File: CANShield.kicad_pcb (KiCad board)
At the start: 4 copper layers, 70 x 59 mm, 92 parts, among them J101 Conn_02x19_Odd_Even, J102 Conn_02x19_Odd_Even, J103 Conn_01x04_Socket, J104 Conn_01x06_Socket, Q101 Si1308EDL, Q102 Si1308EDL, Q103 Si1308EDL, U101 TJA1443ATK/0Z, U102 BD2222G, U103 AT25SF081-XMHD-X, U104 MR20H40

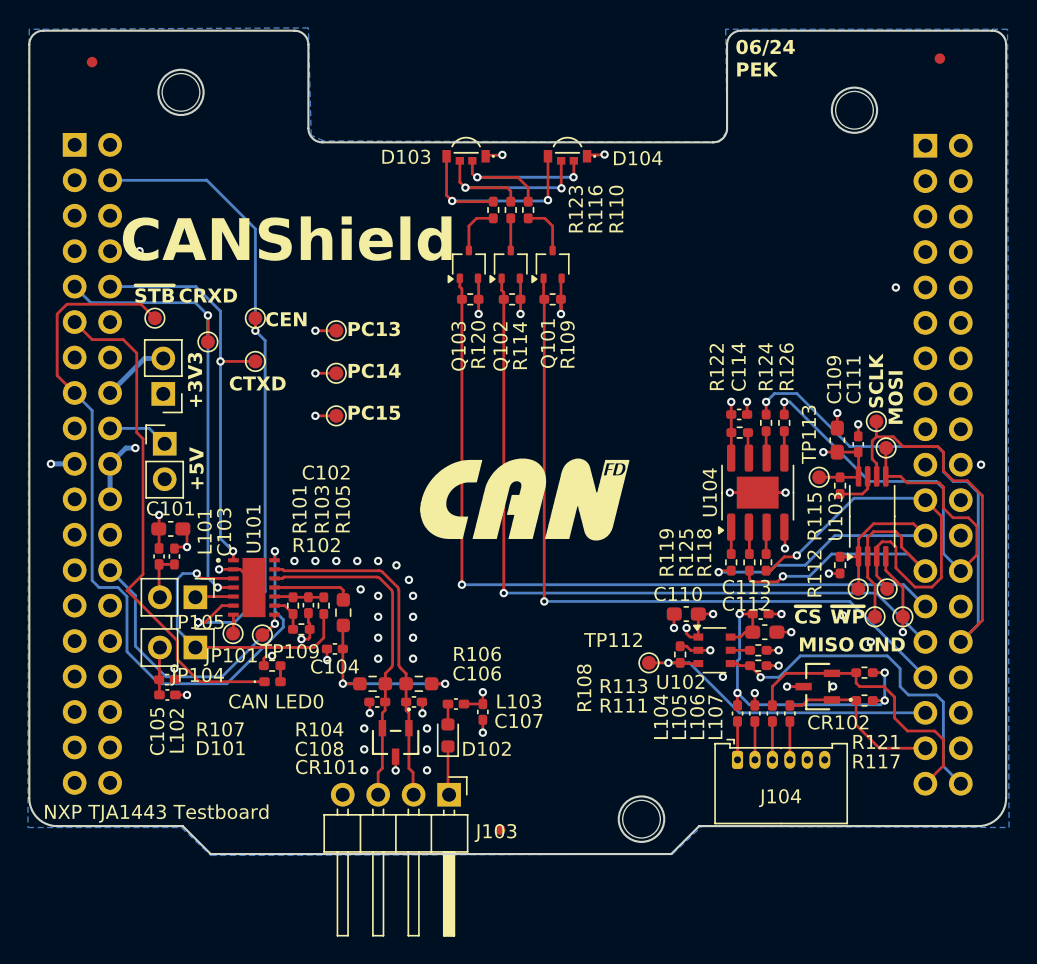
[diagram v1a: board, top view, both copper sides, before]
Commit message: Update BOM
Small changes on pcb layout and update BOM
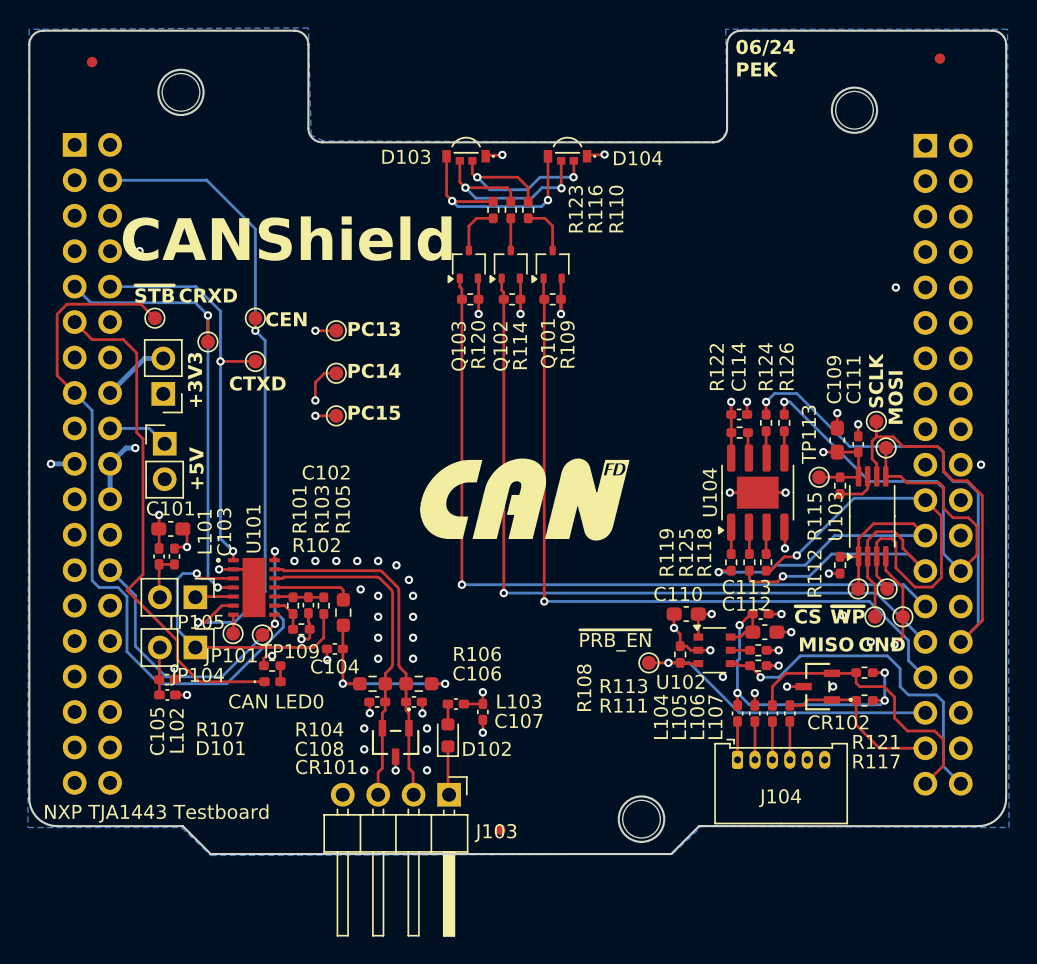
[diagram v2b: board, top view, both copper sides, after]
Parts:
- renumbered TP112 to ~{PRB_EN}
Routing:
- net GND: track 60.7 -> 63.5 mm
- net +5V: track 76.0 -> 74.2 mm, vias 4 -> 3
- net /LED0_RED: track 52.8 -> 53.6 mm
- net /PC14: track 31.3 -> 32.1 mm
- net Net-(D103-RK): track 14.6 -> 15.3 mm
- net /PC15: track 29.1 -> 28.5 mm
- net Net-(D103-GK): track 15.6 -> 16.2 mm
- net /~{WP}: track 30.3 -> 30.8 mm

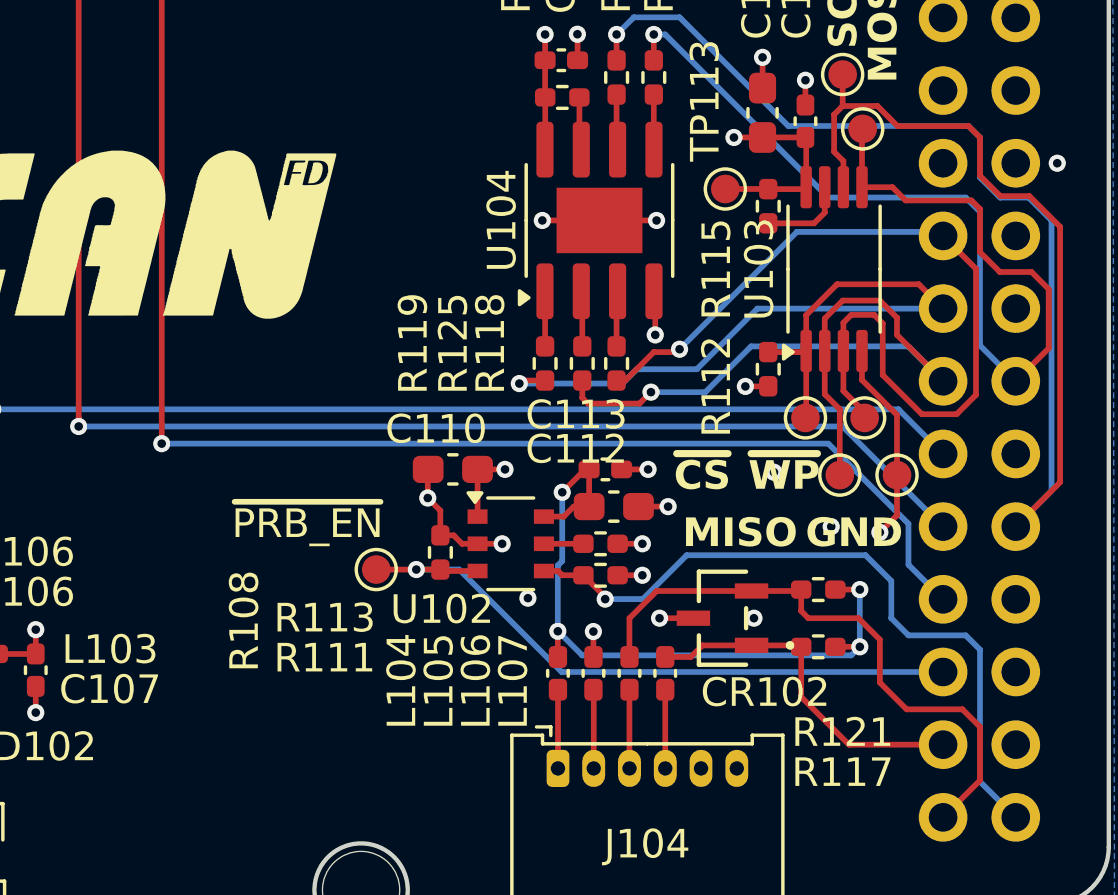
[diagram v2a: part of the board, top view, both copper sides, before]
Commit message: Add bew esd diode
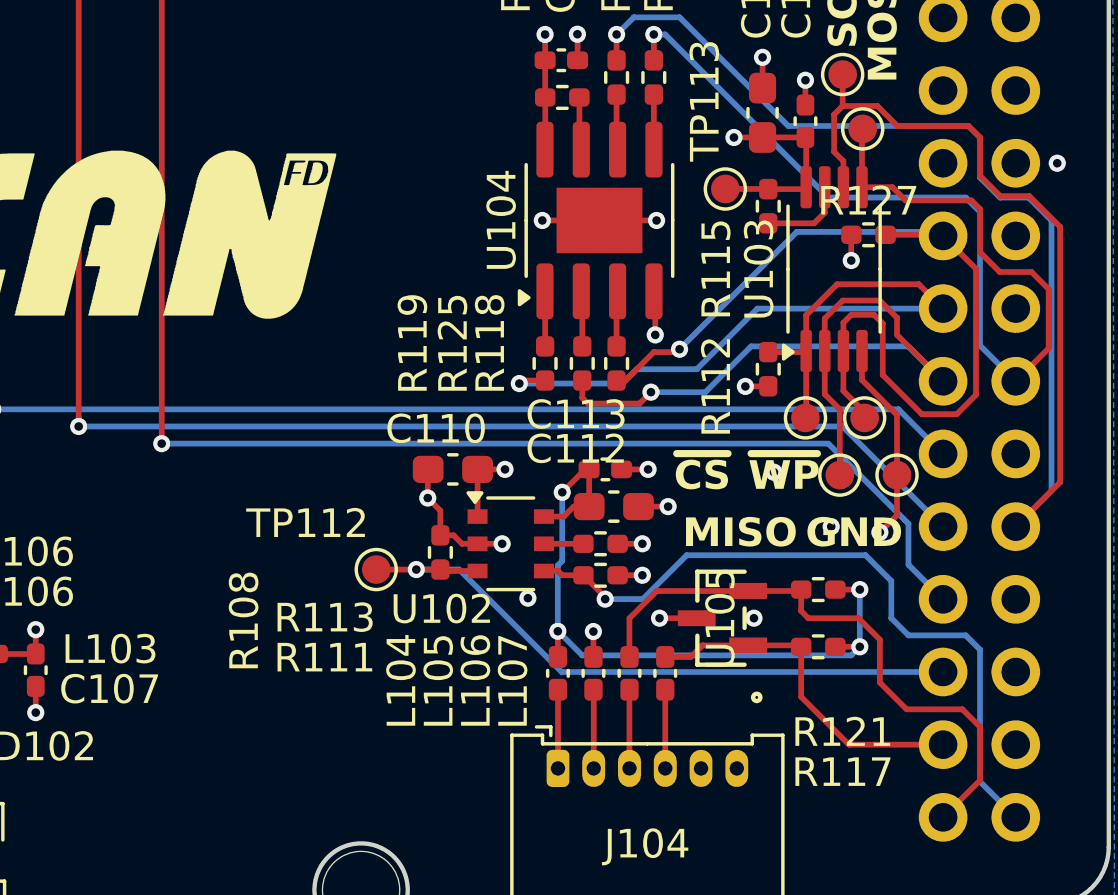
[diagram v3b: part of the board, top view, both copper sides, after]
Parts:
- removed CR102: PESD2CANFD27V-TR, PESD2CANFD27V-TR:SOT23_PESD2_NEX
- added R127: 100k, Resistor_SMD:R_0402_1005Metric_Pad0.72x0.64mm_HandSolder, F.Cu at (161.9, 101.6)
- added U105: PESD5V0S2BT, PESD5V:SOT23_NEX, F.Cu at (156.7, 115.0)
- R116: value 1k -> 680
- R123: value 1k -> 340
- U102: value BD2222G -> BD22441G-C
- U103: value AT25SF081-XMHD-X -> AT25DF041B-XMHNHR-T
- renumbered ~{PRB_EN} to TP112
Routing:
- net /~{WP}: track 30.8 -> 32.8 mm
- net +3V3: track 27.1 -> 28.1 mm, vias 8 -> 9

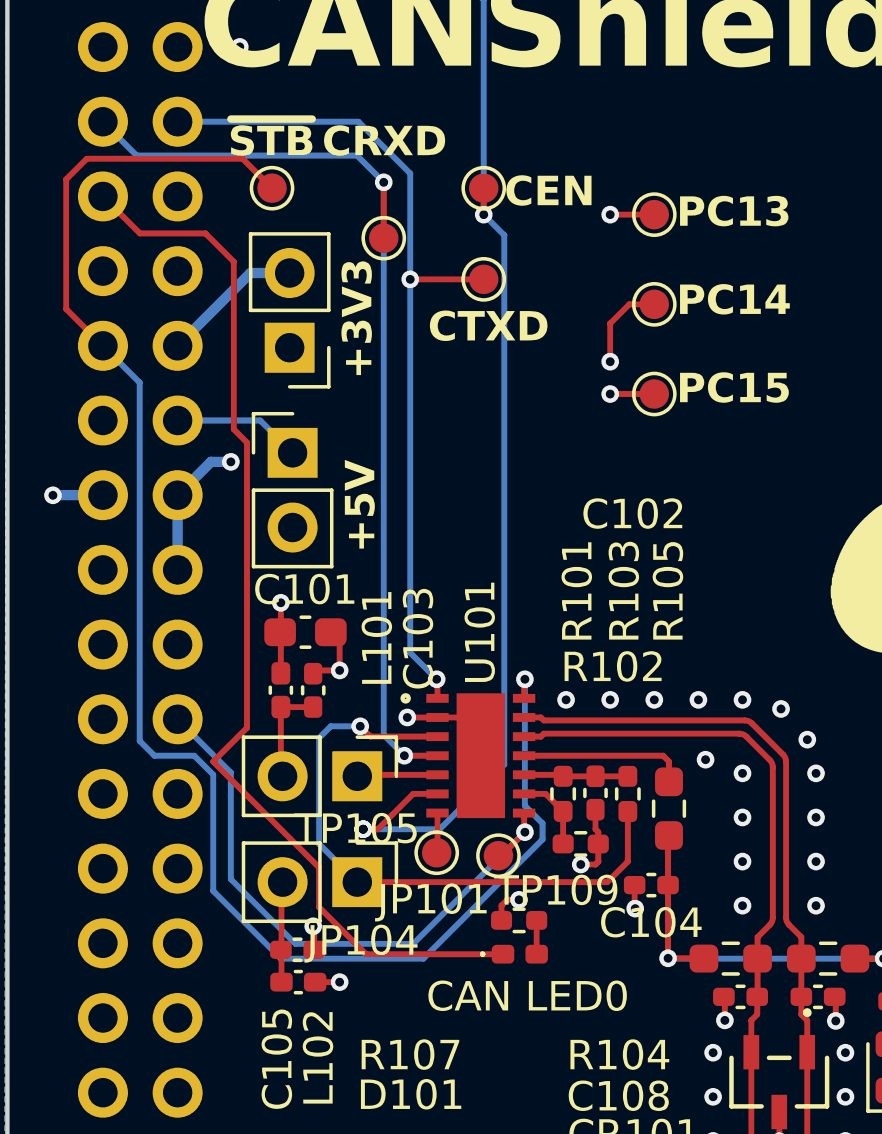
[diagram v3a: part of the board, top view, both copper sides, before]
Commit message: Moved Testpoints
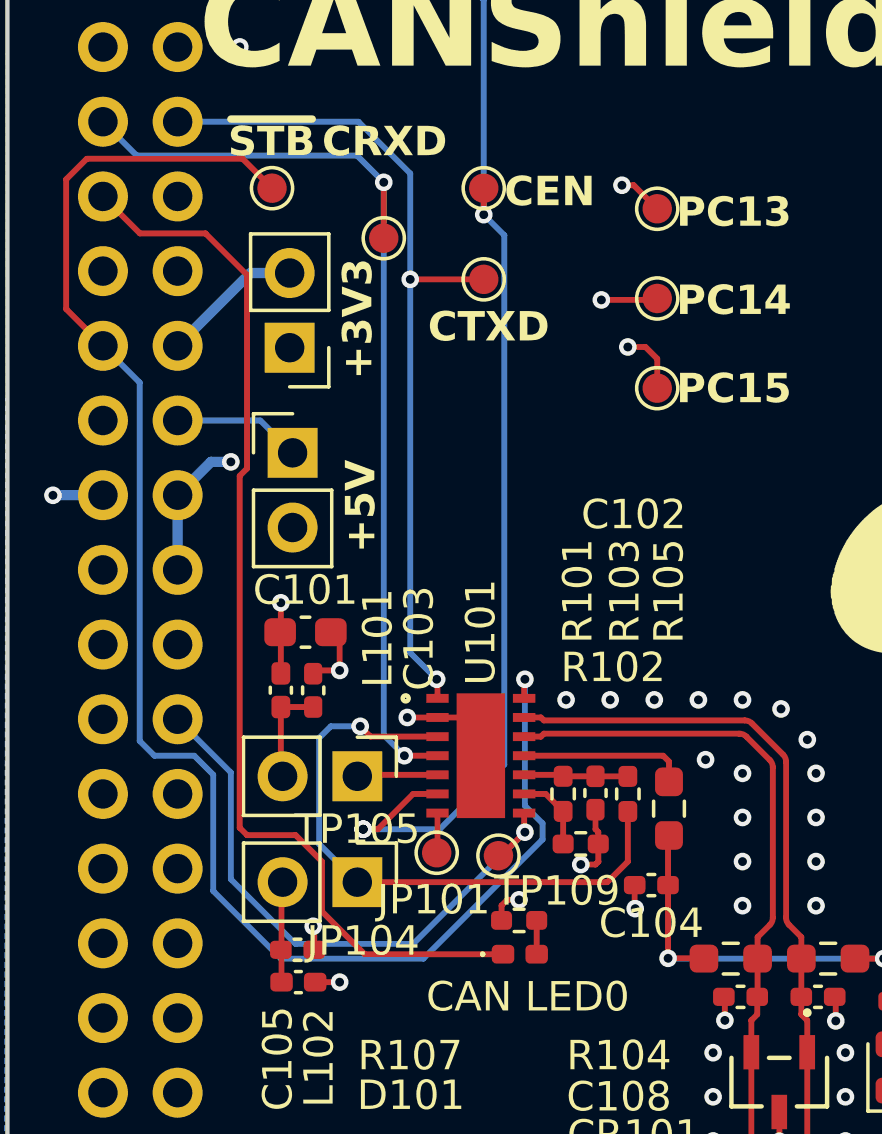
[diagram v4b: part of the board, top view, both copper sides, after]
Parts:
- moved TP101 0.22 mm to (122.3, 89.3)
- moved TP106 0.22 mm to (122.3, 92.3)
- moved TP108 0.22 mm to (122.3, 95.4)
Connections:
- TP101 pad 1: /PC13 -> /PC2
- TP106 pad 1: /PC14 -> /PC3
- TP108 pad 1: /PC15 -> /PF0
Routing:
- net /PC2: track 0.00 -> 56.1 mm, vias 0 -> 1
- net /PC3: track 0.00 -> 53.8 mm, vias 0 -> 1
- net /PF0: track 0.00 -> 48.9 mm, vias 0 -> 1
- net /PC14: track 32.1 -> 0.00 mm, vias 1 -> 0
- net /PC13: track 32.1 -> 0.00 mm, vias 1 -> 0
- net /PC15: track 28.5 -> 0.00 mm, vias 1 -> 0
- net +5V: track 74.2 -> 73.5 mm

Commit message: changes from pcb review
update pcb with remained changes in pcb review.
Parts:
- moved TP109 0.90 mm to (117.8, 111.3)
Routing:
- net GND: track 63.5 -> 75.7 mm, vias 57 -> 59
- net /CAN0_EN: track 47.9 -> 44.6 mm
- net +3V3: track 28.1 -> 24.8 mm
- net +5V: track 73.5 -> 75.2 mm
- net /~{CAN0_ERR}: track 20.6 -> 22.1 mm
- net /~{CAN0_STB}: track 55.0 -> 53.8 mm
- net /CAN0_RXD: track 33.3 -> 34.2 mm
- net /CAN0_LED: track 36.6 -> 36.9 mm, vias 0 -> 1

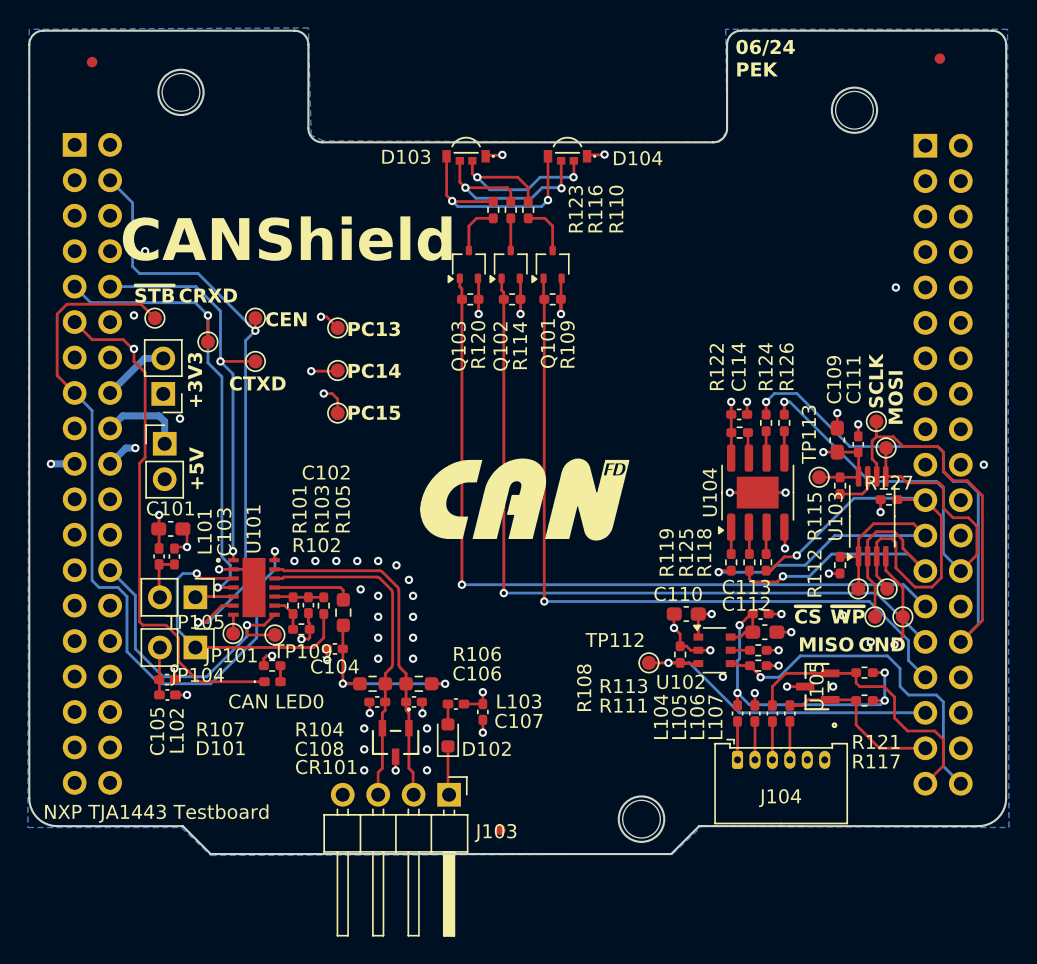
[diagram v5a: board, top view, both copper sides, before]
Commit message: Update CANShield.kicad_pcb
all changes from review. PCB ready for final review.
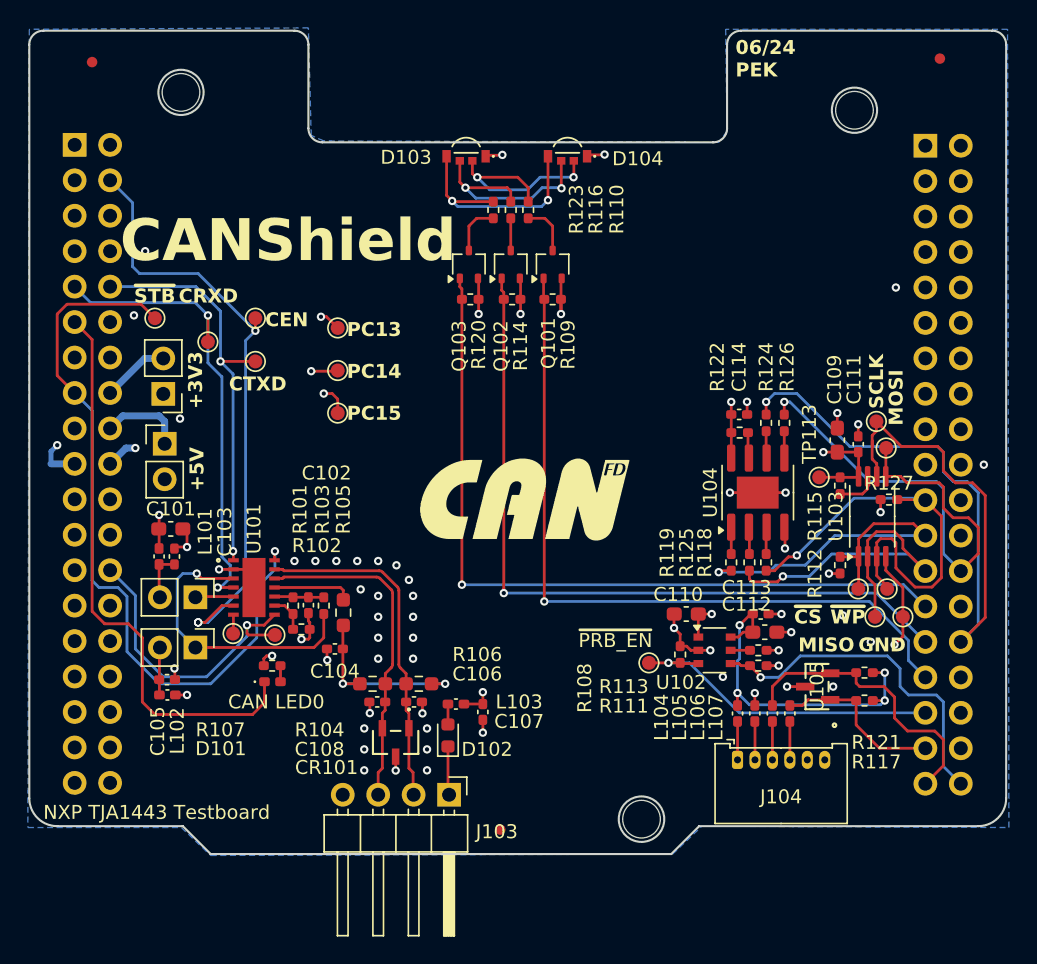
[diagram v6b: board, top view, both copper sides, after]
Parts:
- renumbered TP112 to ~{PRB_EN}
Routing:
- net /CAN0_LED: track 36.9 -> 41.2 mm, vias 1 -> 0
- net +5V: track 75.2 -> 71.1 mm
- net /PF0: track 48.9 -> 52.7 mm
- net /PC2: track 56.1 -> 58.9 mm
- net GND: track 75.7 -> 77.0 mm
- net /SCLK: track 56.8 -> 57.9 mm
- net /PC3: track 53.8 -> 54.5 mm
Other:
- board text added: "CN7"
- board text added: "JLCJLCJLC"
